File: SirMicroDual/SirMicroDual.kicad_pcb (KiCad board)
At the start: 2 copper layers, 50.8 x 20.5 mm, 46 parts, among them J1 Conn_01x16, J2 Conn_01x16, J3 USB_B_Micro, Q1 Q_DUAL_PMOS_S1G1D2S2G2D1, U1 ATmega32U4-MU, U2 AP2127K-3.3, U3 AP1117-50, Y1 Resonator

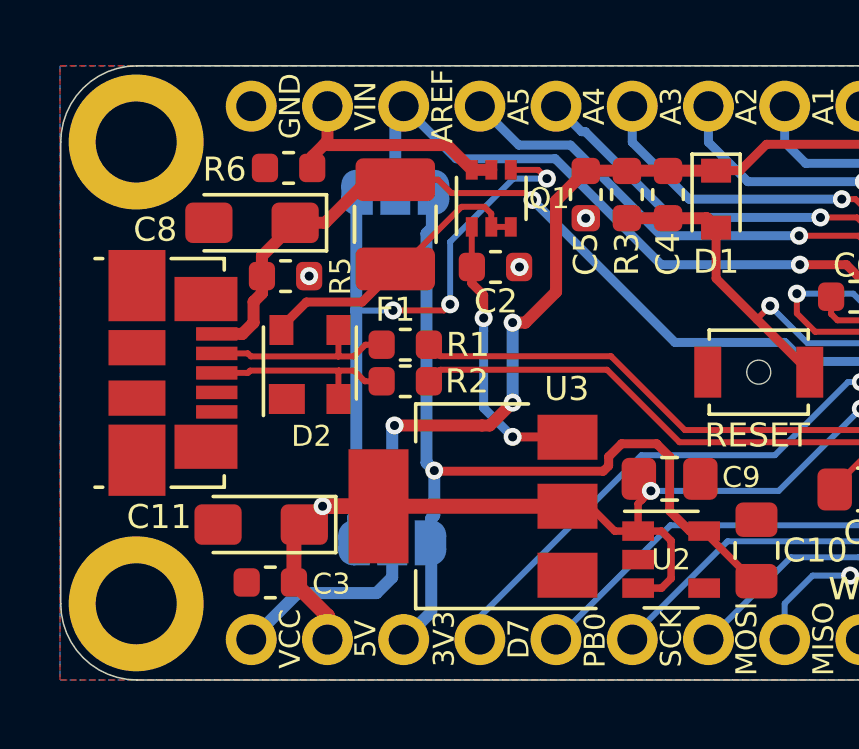
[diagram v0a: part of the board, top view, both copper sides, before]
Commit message: Jumpers Moved
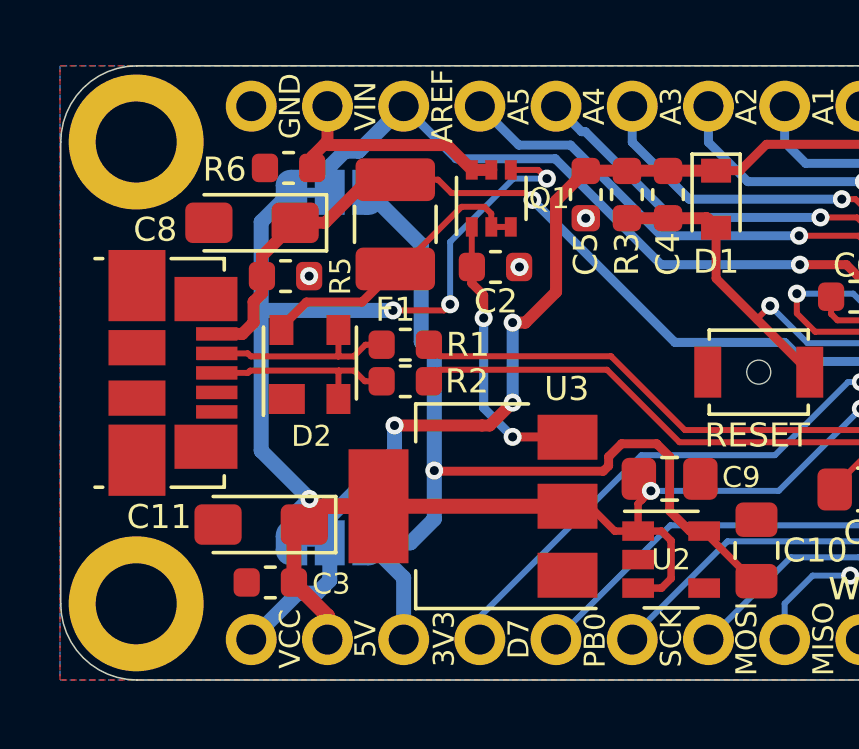
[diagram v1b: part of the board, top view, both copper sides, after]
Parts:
- moved JP2 2.18 mm to (134.9, 85.4)
- moved JP1 2.08 mm to (134.9, 97.1)
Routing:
- net 5V: track 58.6 -> 63.7 mm
- net 3V3: track 29.8 -> 32.3 mm
- net AREF: track 23.2 -> 24.7 mm
- net VCC: track 91.8 -> 90.7 mm

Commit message: Dimensions Updated
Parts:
- J1, J2: moved to F.Cu
- turned J1 to 90 degrees
- turned J2 to 90 degrees

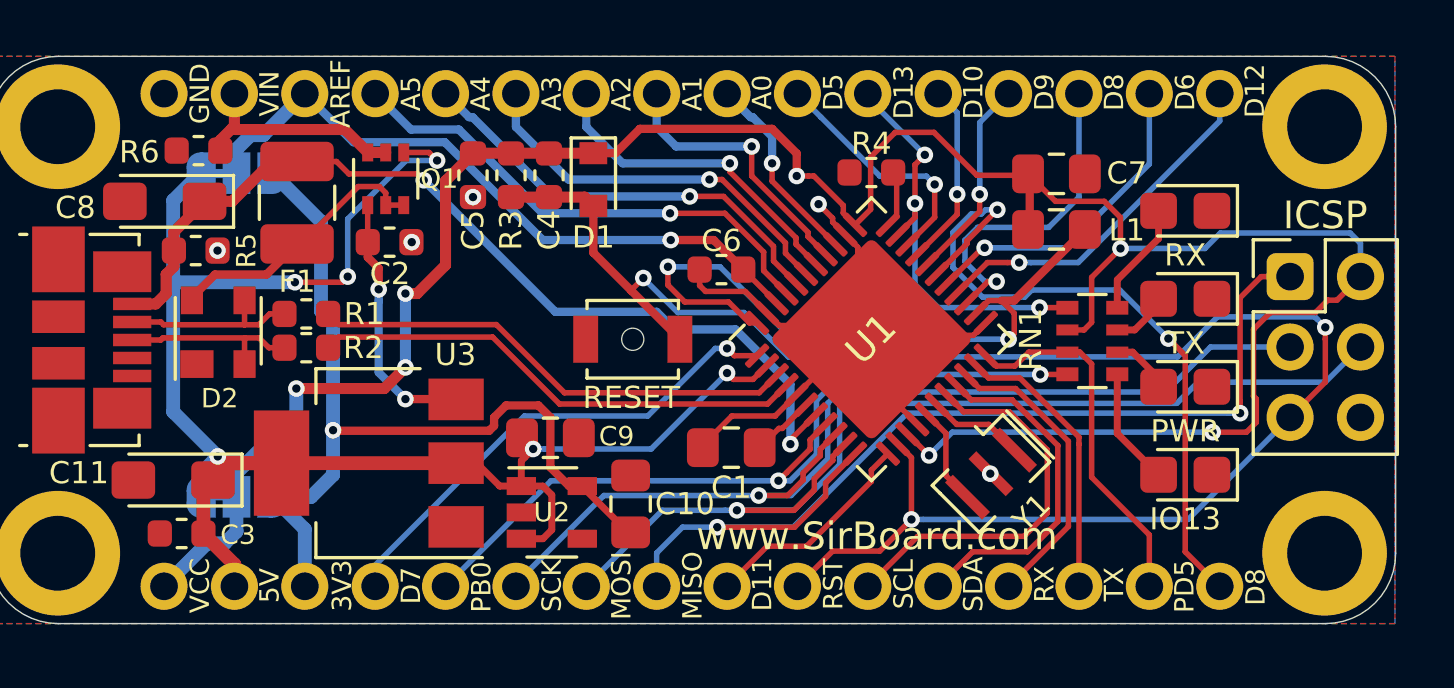
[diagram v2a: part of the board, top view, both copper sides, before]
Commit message: Layout updated and silkscreen revised
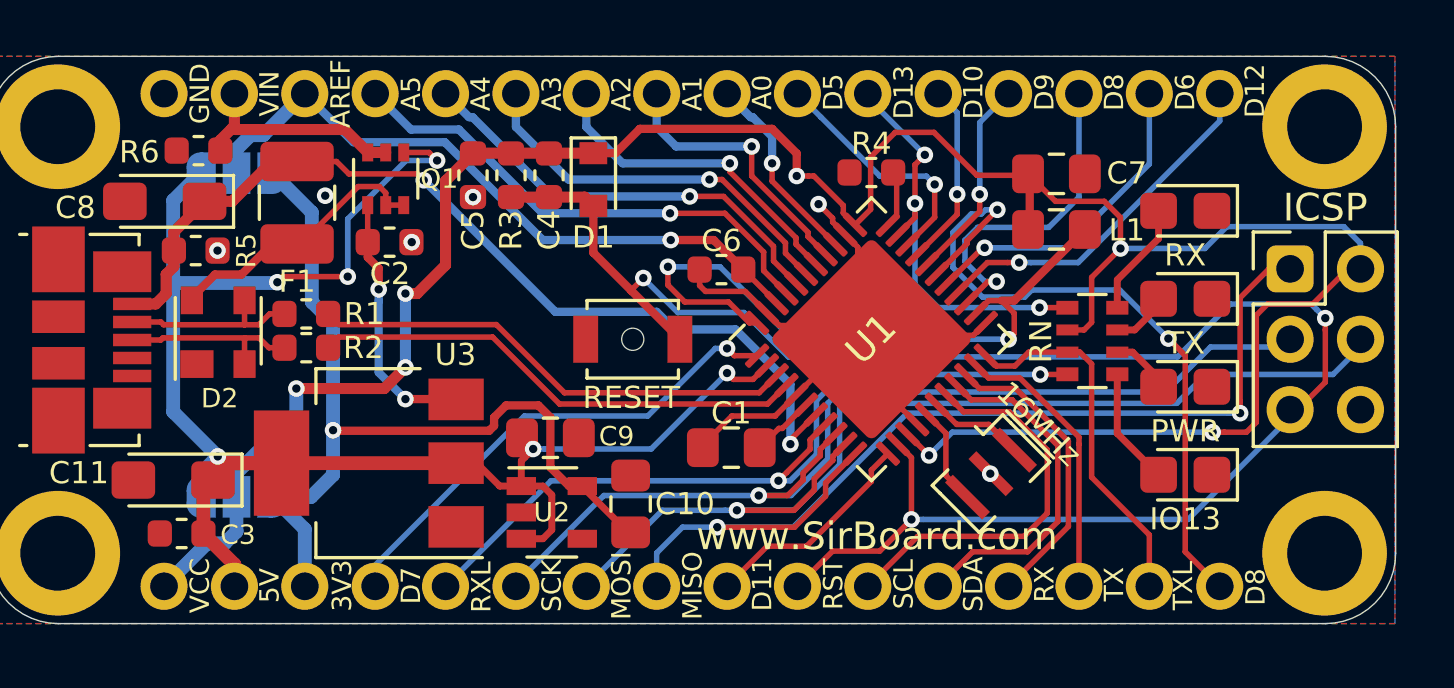
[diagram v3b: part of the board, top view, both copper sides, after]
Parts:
- J1, J2: moved to B.Cu
- JP1, JP2: footprint Jumper:SolderJumper-3_P1.3mm_Bridged12_RoundedPad1.0x1.5mm -> Jumper:SolderJumper-3_P1.3mm_Open_RoundedPad1.0x1.5mm
- moved ICSP 0.28 mm to (172.9, 88.9)
- turned J1 to 270 degrees
- turned J2 to 270 degrees
- renumbered Y1 to 16MHz, RN1 to RN
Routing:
- net 5V: track 63.7 -> 63.0 mm
- net RST: track 63.4 -> 64.0 mm
- net GND: vias 5 -> 6
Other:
- board text added: "RXL"
- board text added: "TXL"
- board text removed: "PB0"
- board text removed: "PD5"

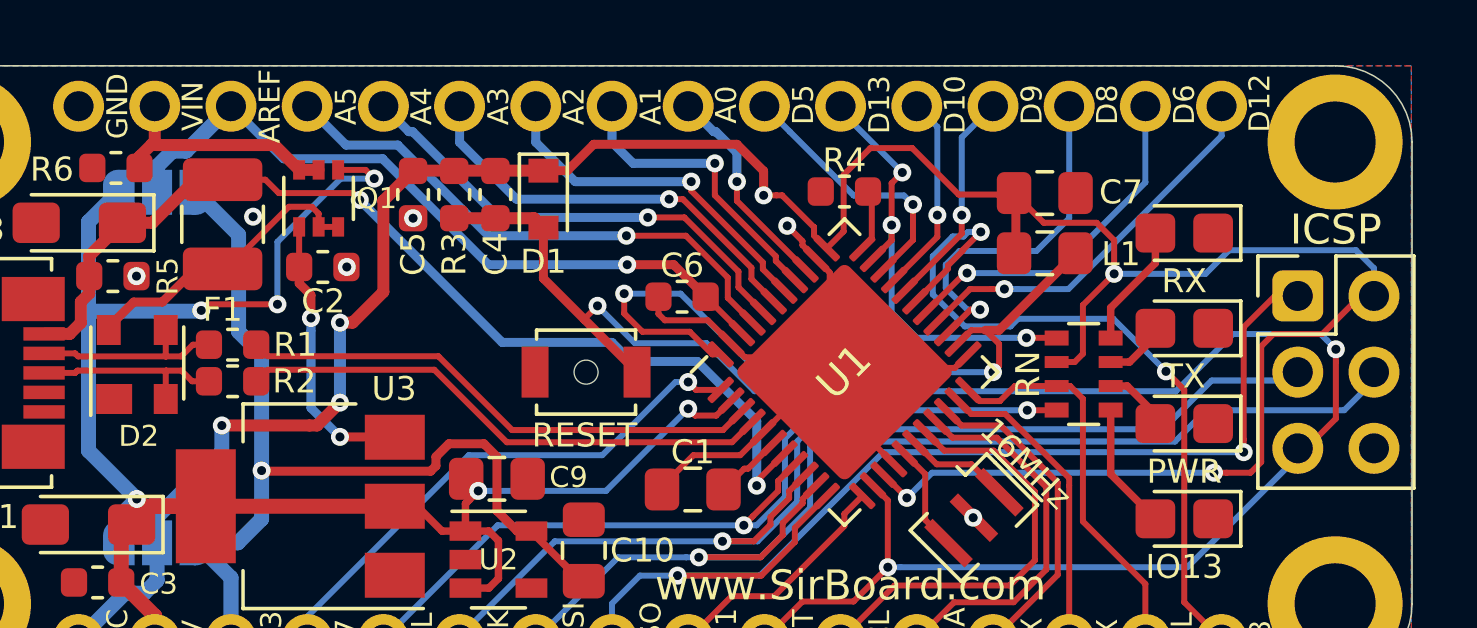
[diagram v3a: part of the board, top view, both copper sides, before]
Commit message: LDO changed
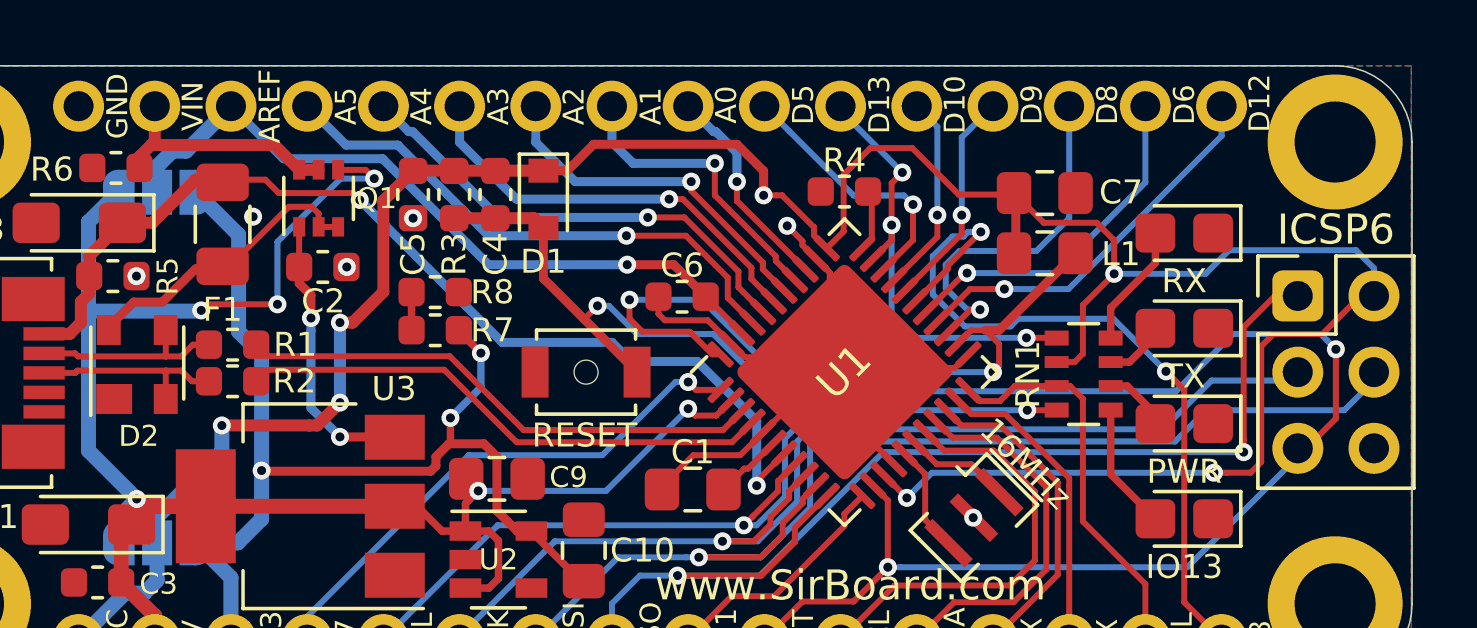
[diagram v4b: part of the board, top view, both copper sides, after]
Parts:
- added R7: 68K, Resistor_SMD:R_0603_1608Metric, F.Cu at (144.1, 90.0)
- added R8: 22K, Resistor_SMD:R_0603_1608Metric, F.Cu at (144.1, 88.8)
- 16MHz: value Resonator -> 16MHz
- F1: footprint Resistor_SMD:R_1210_3225Metric_Pad1.42x2.65mm_HandSolder -> Resistor_SMD:R_1206_3216Metric
- renumbered ICSP to ICSP6, RN to RN1
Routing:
- net 3V3: track 32.3 -> 36.8 mm, vias 1 -> 3
- net Net-(R7-Pad2): track 0.00 -> 1.27 mm
- net Net-(L1-Pad2): track 24.4 -> 23.9 mm

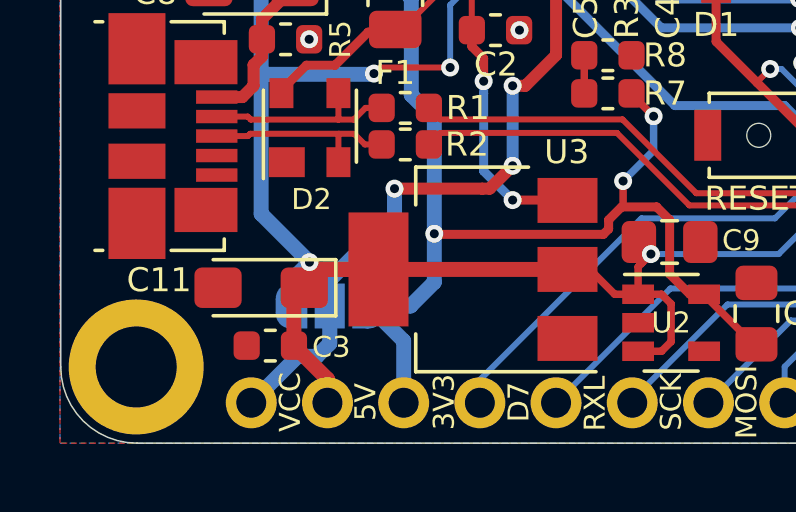
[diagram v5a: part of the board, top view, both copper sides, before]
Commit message: Capacitor Footprint change
3216 to 3512
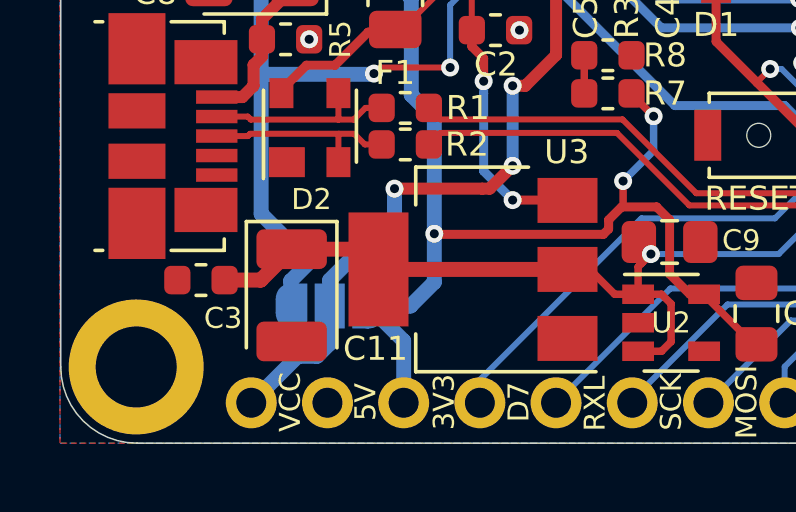
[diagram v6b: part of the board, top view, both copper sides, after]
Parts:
- C11: footprint Capacitor_Tantalum_SMD:CP_EIA-3216-18_Kemet-A_Pad1.58x1.35mm_HandSolder -> Capacitor_Tantalum_SMD:CP_EIA-3528-12_Kemet-T
- moved C3 3.18 mm to (130.6, 96.3)
- moved C11 1.05 mm to (133.6, 96.8), turned to 270 degrees
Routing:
- net 5V: track 63.0 -> 57.4 mm, vias 6 -> 5
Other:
- rule pad_to_mask_clearance: 0.051 -> 0
- rule solder_mask_min_width: 0.25 -> 0.1

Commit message: Part Numbers Added
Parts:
- removed R7: 68K, Resistor_SMD:R_0603_1608Metric
- removed R8: 22K, Resistor_SMD:R_0603_1608Metric
- JP1, JP2: value SolderJumper_3_Bridged12 -> SolderJumper_3_Open
- Q1: value Q_DUAL_PMOS_S1G1D2S2G2D1 -> DMP2004DWK-7
- U3: value AP1117-50 -> AZ1117-5.0
- moved C11 96.3 mm to (51.3, 46.7)
- moved REF** 96.2 mm to (46.1, 49.3)
- moved REF** 96.2 mm to (46.1, 33.9)
- moved 16MHz 96.2 mm to (79.8, 46.4)
- moved C10 96.2 mm to (66.8, 47.5)
- moved C2 96.2 mm to (58.1, 38.0)
- moved C3 96.2 mm to (48.3, 46.4)
- moved C7 96.2 mm to (82.2, 35.6)
- moved C9 96.2 mm to (63.9, 45.1)
- moved D1 96.2 mm to (65.5, 35.8)
- moved D2 96.2 mm to (51.9, 41.2)
- moved F1 96.2 mm to (54.8, 36.6)
- moved G*** 96.2 mm to (51.2, 41.3)
- moved IO13 96.2 mm to (86.8, 46.4)
- moved J1 96.2 mm to (50.0, 32.7)
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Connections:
- C11 pad 1: 5V -> Net-(C11-Pad1)
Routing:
- net Net-(C11-Pad1): track 9.40 -> 17.3 mm, vias 2 -> 3
- net 5V: track 57.4 -> 65.1 mm, vias 5 -> 6
- net 3V3: track 36.8 -> 32.6 mm, vias 3 -> 1
- net Net-(R7-Pad2): track 1.27 -> 0.00 mm
